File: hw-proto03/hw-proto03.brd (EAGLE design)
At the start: 54.3 x 62.2 mm, 30 parts, among them IC2 IR4427S, IC3 MCP2562T, IC5 IR4427S, J1 000, J2 000, J3 000, J4 000, Q1 SQJ147ELP-T1_GE3, Q2 SQJ147ELP-T1_GE3, Q3 SQJ147ELP-T1_GE3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

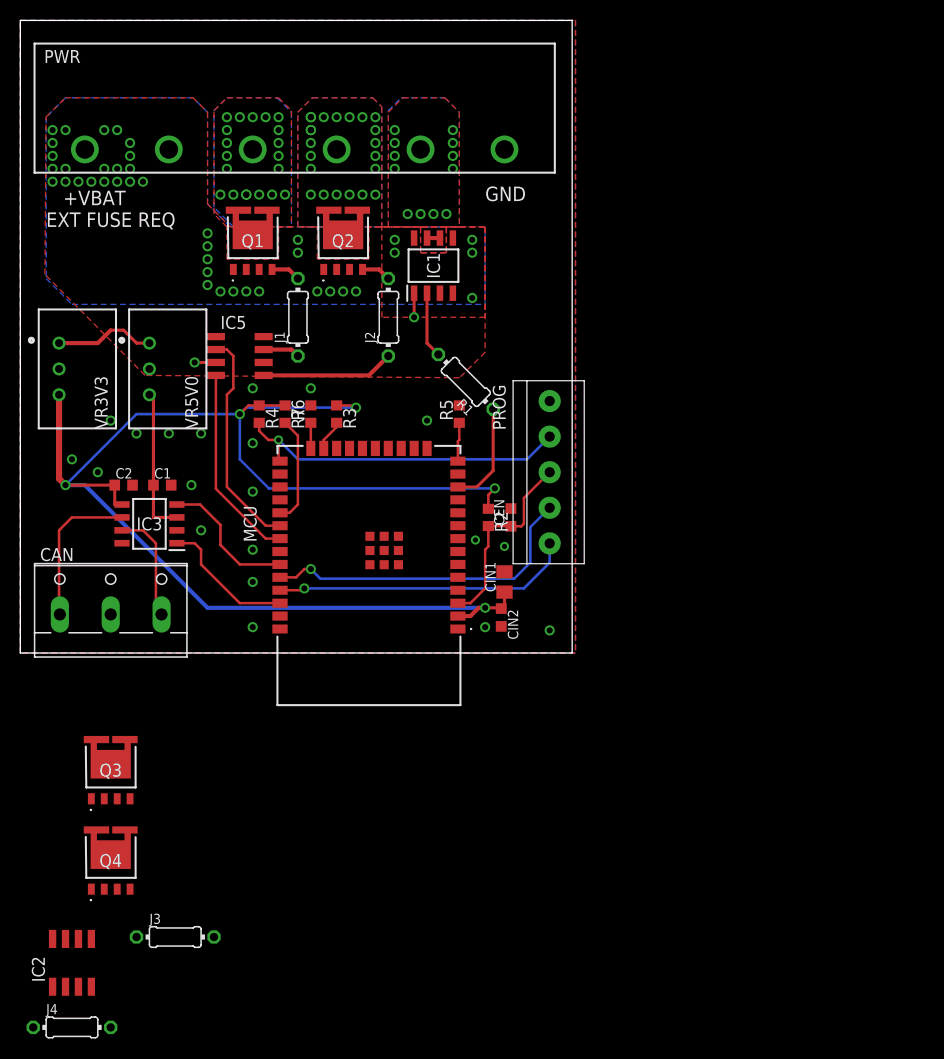
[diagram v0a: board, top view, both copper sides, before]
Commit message: big layout - 6 switches
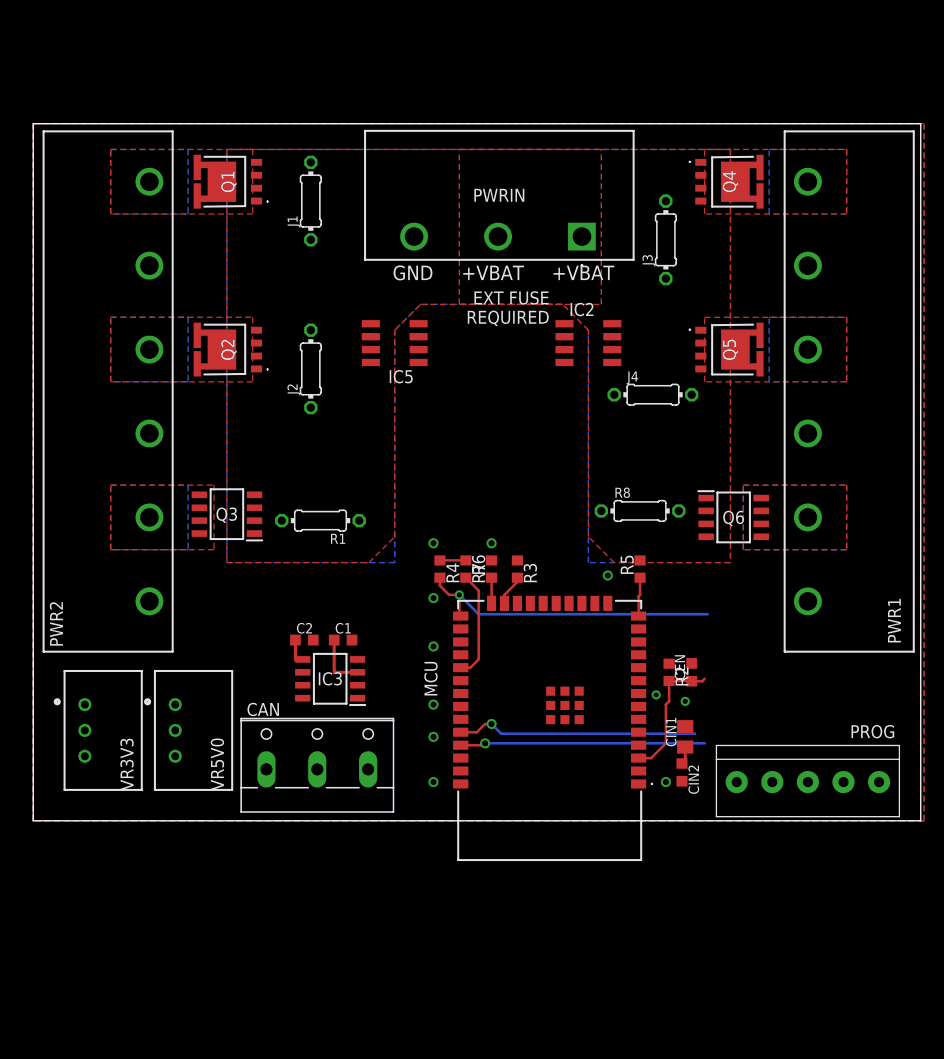
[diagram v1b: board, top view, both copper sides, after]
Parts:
- removed IC1: (no value), VN5E160MSTR-E:SOIC127P600X175-8N
- removed PWR: (no value), 4DB-P108-06:4DBP10806
- added PWR1, PWR2: (no value), 4DB-P108-06:4DBP10806
- added PWRIN: (no value), con-barrier-3pos:4DBP10803
- added Q5: SQJ147ELP-T1_GE3, transistor-vishay-pchan-pso8:SQJ147ELPT1_GE3
- added Q6: (no value), VN5E160MSTR-E:SOIC127P600X175-8N
- added R8: 10K0, rcl:0204/7
- Q3: value SQJ147ELP-T1_GE3 -> (none); device transistor-vishay-pchan-pso8:SQJ147ELPT1_GE3 -> VN5E160MSTR-E:SOIC127P600X175-8N
- moved Q4 90.3 mm to (69.8, 64.1), turned to 270 degrees
- moved J4 84.5 mm to (62.2, 43.2)
- moved J3 83.9 mm to (63.5, 58.4), turned to 90 degrees
- moved IC2 79.4 mm to (55.9, 48.3), turned to 270 degrees
- moved PROG 39.7 mm to (77.5, 5.08), turned to 180 degrees
- moved VR3V3 35.7 mm to (6.35, 10.2)
- moved VR5V0 35.7 mm to (15.2, 10.2)
- moved Q3 27.6 mm to (20.3, 31.4), turned to 180 degrees
- moved CAN 25.4 mm to (29.2, 7.62)
- moved CEN 23.4 mm to (66.0, 15.9)
- moved CIN2 23.4 mm to (65.1, 6.03)
- moved C1 23.4 mm to (31.8, 19.1)
- moved C2 23.4 mm to (27.9, 19.1)
- moved CIN1 23.4 mm to (65.4, 9.53)
- moved IC3 23.4 mm to (30.5, 15.2)
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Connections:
- new net CTL5: IC2.4
- new net CTL6: R8.1
- new net N$12: Q6.2, R8.2
- new net SW4: PWR1.1, Q4.5, Q4.6, Q4.7, Q4.8, Q4.9
- new net SW5: PWR1.3, Q5.5, Q5.6, Q5.7, Q5.8, Q5.9
- new net SW6: PWR1.5, Q6.6, Q6.7
- net +12V: now also PWRIN.1, PWRIN.2, Q3.5, Q3.8, Q5.1, Q5.2, Q5.3, Q6.5, Q6.8; no longer IC1.5, IC1.8, PWR.1, PWR.2, Q3.1, Q3.2, Q3.3
- net CTL1: no longer IC2.2
- net CTL2: no longer IC2.4
- net CTL4: now also IC2.2
- net GND: now also PWR1.2, PWR1.4, PWR1.6, PWR2.1, PWR2.3, PWR2.5, PWRIN.3, Q3.1, Q6.1; no longer IC1.1, PWR.6
- net N$10: now also Q4.4; no longer Q3.4
- net N$11: now also Q5.4; no longer Q4.4
- net N$7: now also Q3.2; no longer IC1.2
- net SW1: now also PWR2.6; no longer PWR.3, Q3.5, Q3.6, Q3.7, Q3.8, Q3.9
- net SW2: now also PWR2.4; no longer PWR.4, Q4.5, Q4.6, Q4.7, Q4.8, Q4.9
- net SW3: now also PWR2.2, Q3.6, Q3.7; no longer IC1.6, IC1.7, PWR.5
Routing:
- net +3V3: track 140.9 -> 6.91 mm, vias 5 -> 0
- net CTL1: track 21.9 -> 0.00 mm
- net CTL2: track 19.9 -> 0.00 mm
- net N$2: track 15.0 -> 0.00 mm
- net CAN_RX: track 13.7 -> 0.00 mm
- net CAN_TX: track 13.4 -> 0.00 mm
- net N$3: track 13.0 -> 0.00 mm
- net N$1: track 11.1 -> 0.00 mm
- net CTL3: track 10.2 -> 0.00 mm
- net +12V: track 9.94 -> 0.00 mm, vias 41 -> 0
- net +5V: track 14.5 -> 5.48 mm
- net RXD0: track 32.2 -> 23.8 mm
- net N$7: track 6.49 -> 0.00 mm
- net EN: track 19.3 -> 13.1 mm
- net TXD0: track 29.5 -> 24.1 mm
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- added copper zone on layer 1, net SW4
- added copper zone on layer 16, net SW4
- added copper zone on layer 1, net SW5
- added copper zone on layer 16, net SW5
- added copper zone on layer 1, net SW6
- added copper zone on layer 16, net SW6
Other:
- board size 54.3 x 62.2 mm -> 87.3 x 68.6 mm
- board text added: "+VBAT"
- board text added: "EXT FUSE REQUIRED"
- board text removed: "+VBAT EXT FUSE REQ"

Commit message: layout continues
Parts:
- J1: value 000 -> J15MM; device rcl:0204/7 -> jumper:15
- J2, J4: value 000 -> J5MM; device rcl:0204/7 -> jumper:05
- J3: value 000 -> J12MM; device rcl:0204/7 -> jumper:12
- R8: device rcl:0204/7 -> rcl:0207/12
- moved R8 7.41 mm to (64.8, 25.4), turned to 90 degrees
- moved J1 4.58 mm to (31.1, 58.4)
- moved J3 2.84 mm to (62.2, 55.9)
- moved J2 2.01 mm to (29.2, 47.6), turned to 180 degrees
- moved J4 1.27 mm to (62.2, 44.5)
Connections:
- removed net N$3: IC5.5, J2.1
- new net N$13: IC5.7, J2.1
- net CTL1: now also IC5.4; no longer IC5.2
- net CTL2: now also IC5.2, MCU.26; no longer IC5.4, MCU.31
- net CTL3: now also MCU.31; no longer MCU.12
- net CTL4: now also MCU.12; no longer MCU.11
- net CTL5: now also MCU.11
- net CTL6: now also MCU.10
- net N$4: now also IC5.5; no longer IC5.7
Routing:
- net CTL1: track 0.00 -> 41.3 mm
- net CTL5: track 0.00 -> 37.3 mm, vias 0 -> 2
- net CTL4: track 0.00 -> 36.7 mm, vias 0 -> 2
- net CTL2: track 0.00 -> 32.9 mm
- net CTL3: track 0.00 -> 21.9 mm
- net N$5: track 0.00 -> 7.88 mm
- net N$10: track 0.00 -> 4.71 mm
- net N$6: track 0.00 -> 4.60 mm
- net N$9: track 0.00 -> 4.26 mm
- net N$4: track 0.00 -> 3.63 mm
- net N$13: track 0.00 -> 2.73 mm
- net N$11: track 0.00 -> 2.69 mm
- net N$7: track 0.00 -> 2.69 mm
- net N$8: track 0.00 -> 2.51 mm
- net SW1: track 0.00 -> 1.59 mm, vias 0 -> 30

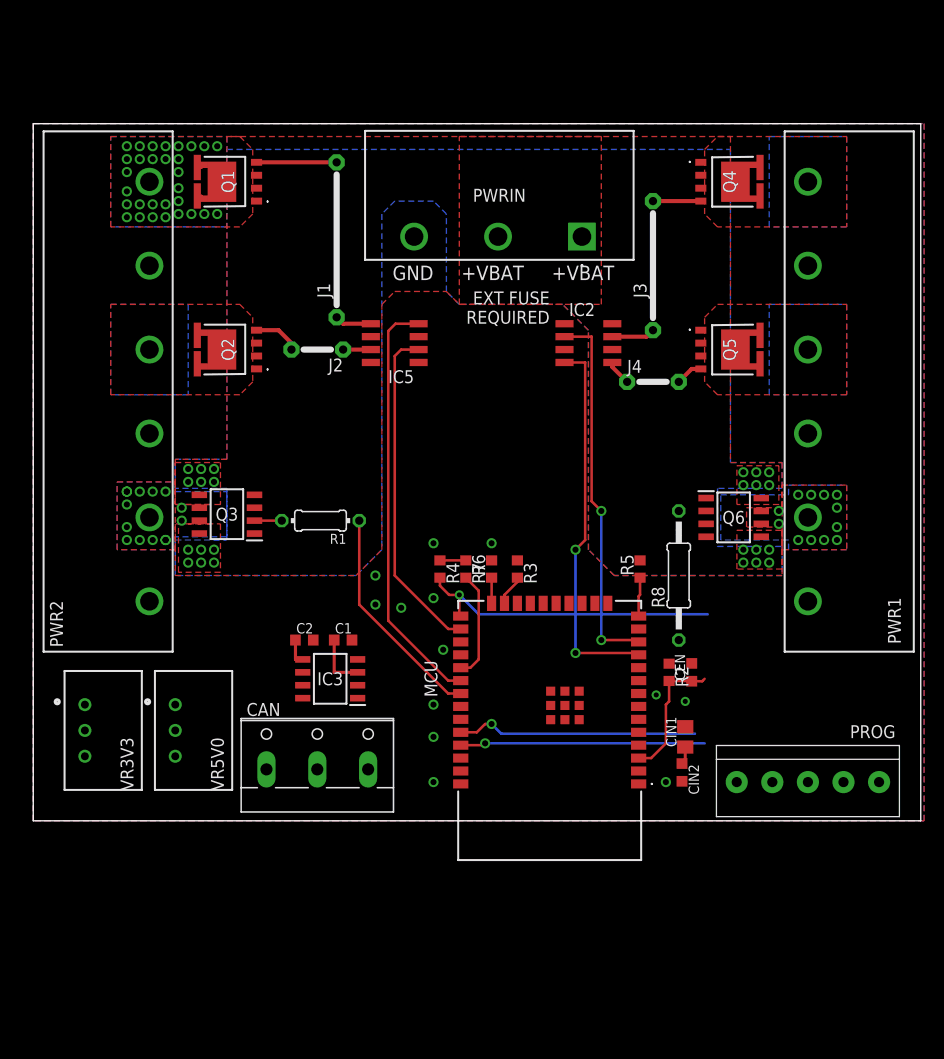
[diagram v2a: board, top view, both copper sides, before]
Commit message: 2nd pass layout and routing complete, needs optimizing
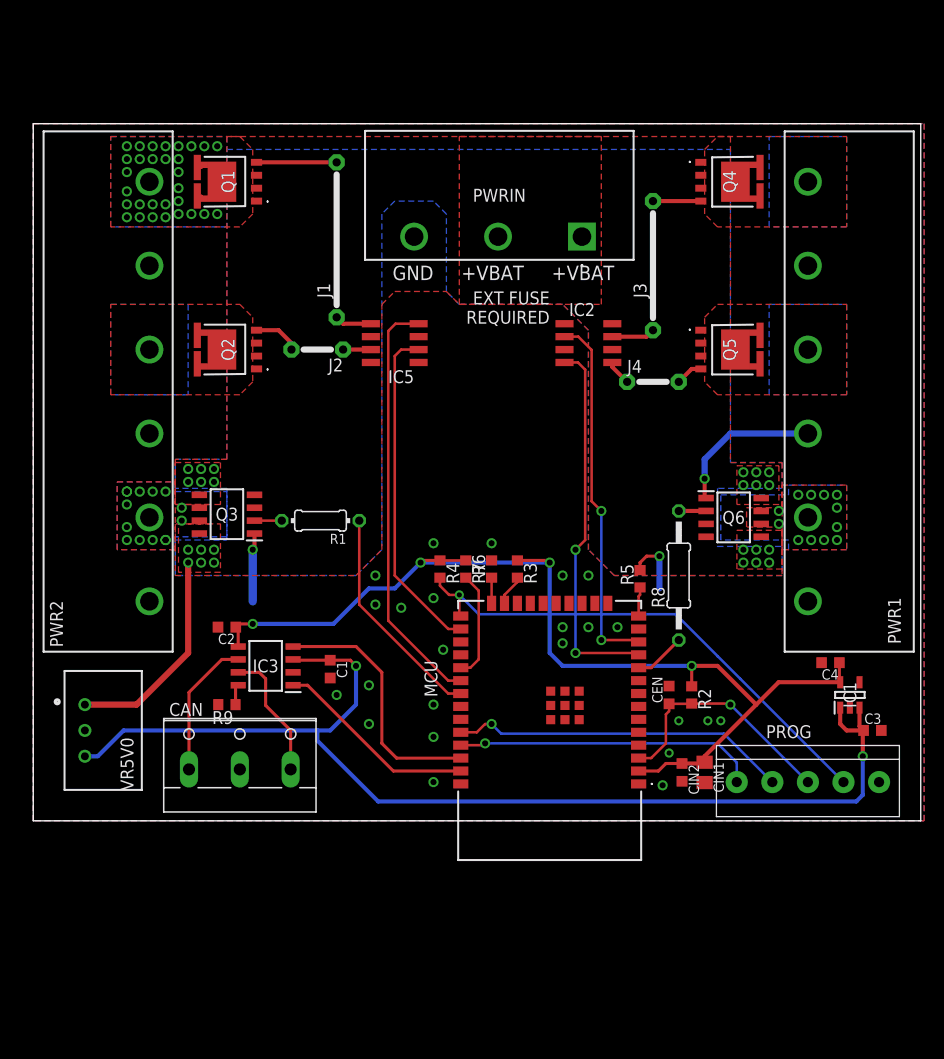
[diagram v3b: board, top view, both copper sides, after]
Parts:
- removed VR3V3: +3V3, TSR_1-2433E:TSR-1-2433
- added C3, C4: 1u, rcl:C0603K
- added IC1: TLV74333PDBVR, TLV74333PDBVR:SOT95P280X145-5N
- added R9: 10K0, rcl:R0603
- moved VR5V0 8.89 mm to (6.35, 10.2)
- moved C2 7.73 mm to (20.3, 20.3), turned to 180 degrees
- moved CAN 7.62 mm to (21.6, 7.62)
- moved IC3 6.48 mm to (24.1, 16.5)
- moved CIN1 3.98 mm to (67.3, 6.03), turned to 270 degrees
- moved CEN 3.14 mm to (63.8, 13.7)
- moved R2 3.14 mm to (66.0, 13.7)
- moved C1 3.13 mm to (30.5, 16.2), turned to 270 degrees
- moved R5 0.95 mm to (61.0, 25.1)
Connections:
- new net CANSTBY: IC3.8, R9.1
- net +12V: no longer VR3V3.1
- net +3V3: now also C4.1, IC1.5; no longer VR3V3.3
- net +5V: now also C3.1, IC1.1, IC1.3
- net CAN_RX: now also MCU.36; no longer MCU.33
- net CAN_TX: now also MCU.37; no longer MCU.36
- net GND: now also C3.2, C4.2, CAN.2, IC1.2, R9.2; no longer VR3V3.2
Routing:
- net +5V: track 5.48 -> 109.4 mm, vias 0 -> 2
- net +3V3: track 6.91 -> 102.3 mm, vias 0 -> 4
- net GND: track 0.00 -> 27.9 mm, vias 13 -> 27
- net CAN_RX: track 0.00 -> 25.1 mm
- net +12V: track 0.00 -> 21.2 mm
- net GPIO0: track 30.5 -> 50.7 mm
- net CAN_TX: track 0.00 -> 20.0 mm
- net N$2: track 0.00 -> 13.8 mm
- net N$1: track 0.00 -> 12.9 mm
- net EN: track 13.1 -> 24.1 mm, vias 0 -> 1
- net RXD0: track 23.8 -> 33.4 mm
- net TXD0: track 24.1 -> 29.9 mm
- net CTL6: track 0.00 -> 5.08 mm
- net N$12: track 0.00 -> 2.69 mm
- net CANSTBY: track 0.00 -> 2.16 mm
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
